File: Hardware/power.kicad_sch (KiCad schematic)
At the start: 17 parts, among them J1 I2C Debug, J2 I2C, J3 I2C, U3 LM285D-2.5, U7 AP7312-1833W6-7

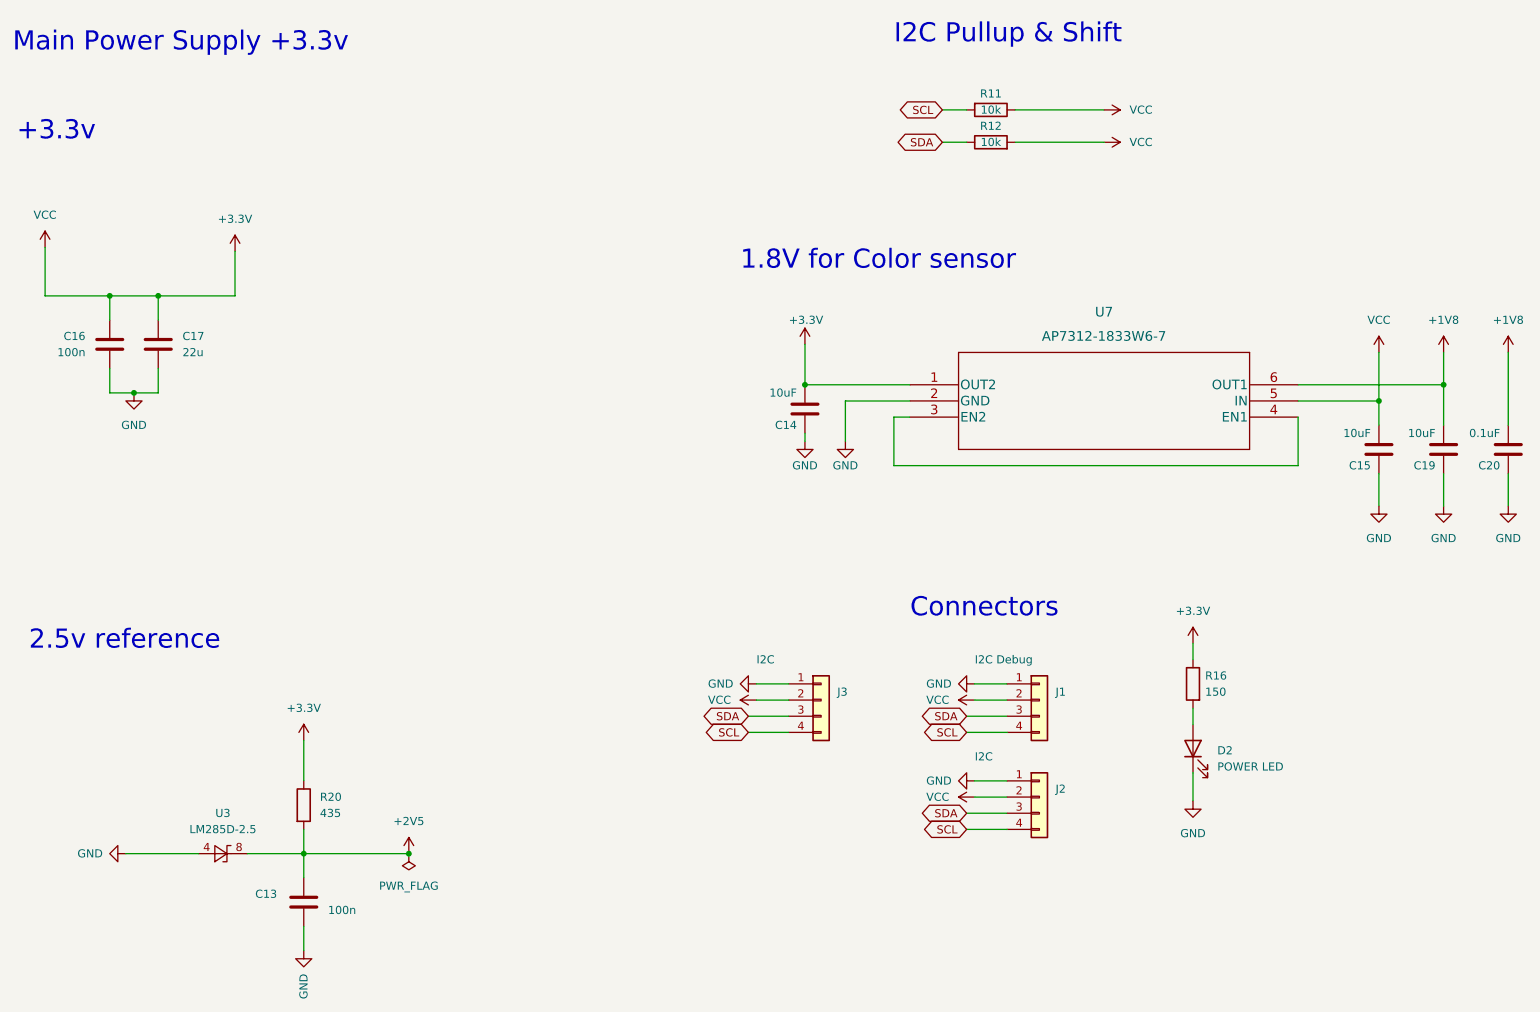
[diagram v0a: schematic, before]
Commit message: Version 0.6 - 4 layer version
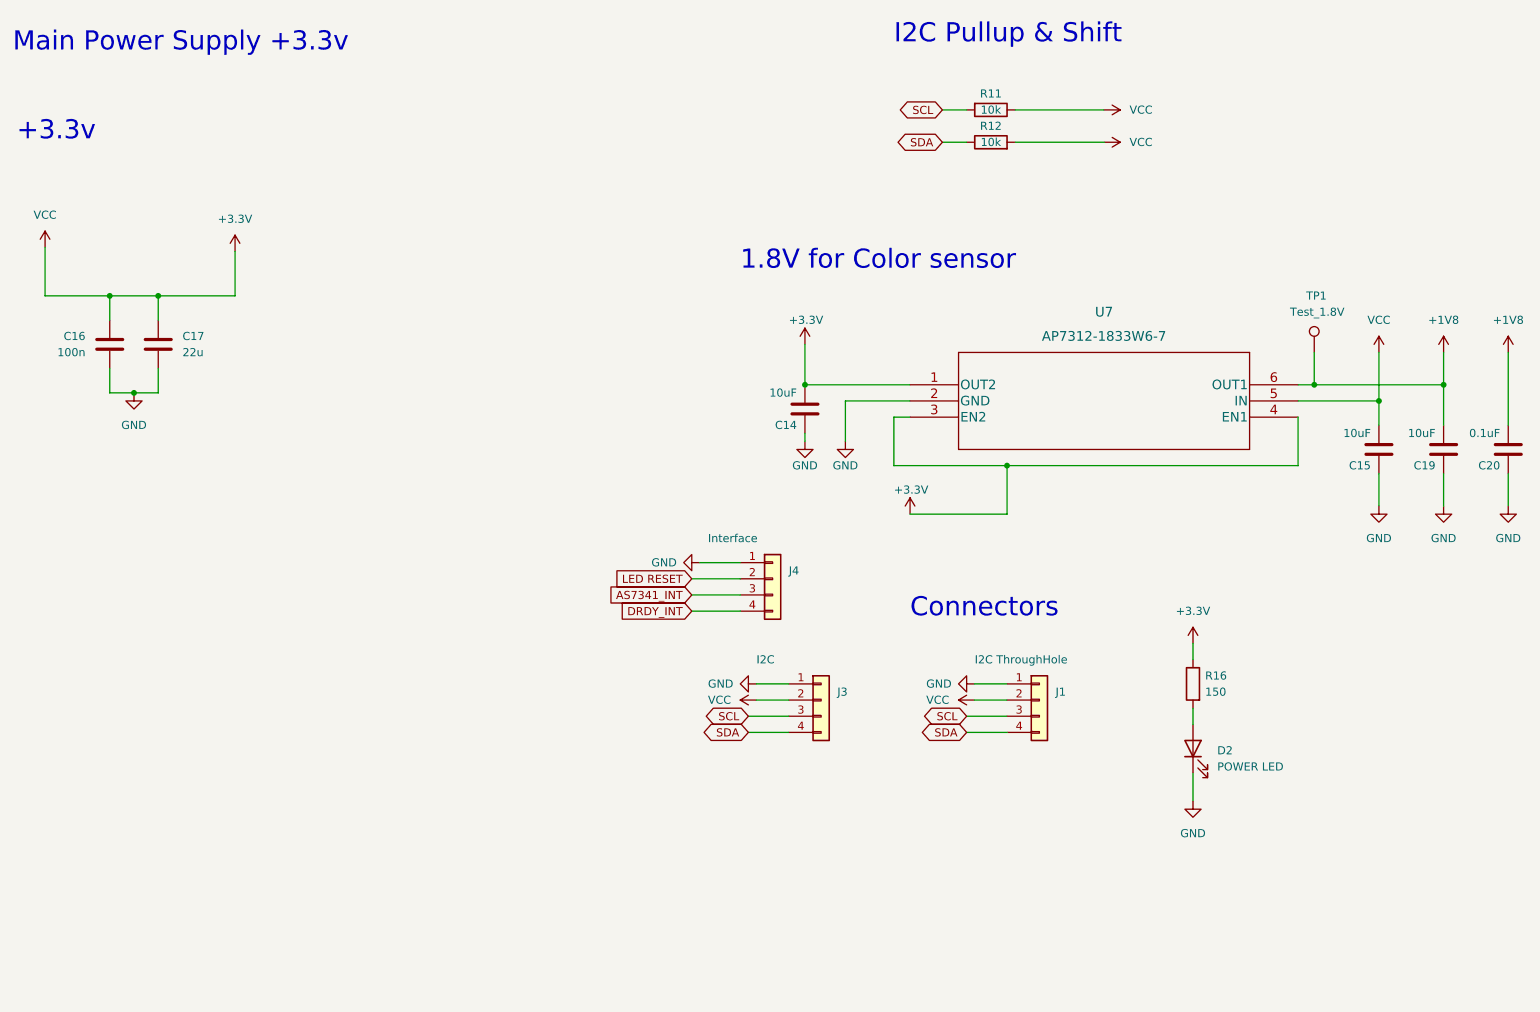
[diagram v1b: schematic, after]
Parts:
- removed C13: 100n, Capacitor_SMD:C_0603_1608Metric_Pad1.08x0.95mm_HandSolder, symbol Device:C
- removed J2: I2C, Connector_JST:JST_SH_SM04B-SRSS-TB_1x04-1MP_P1.00mm_Horizontal, symbol Connector_Generic:Conn_01x04
- removed R20: 435, Resistor_SMD:R_0603_1608Metric_Pad0.98x0.95mm_HandSolder, symbol Device:R
- removed U3: LM285D-2.5, Package_SO:SOIC-8_3.9x4.9mm_P1.27mm, symbol Reference_Voltage:LM285D-2.5
- added J4: Interface, Connector_PinSocket_2.54mm:PinSocket_1x04_P2.54mm_Vertical, symbol Connector_Generic:Conn_01x04
- added TP1: Test_1.8V, TestPoint:TestPoint_Pad_D1.5mm, symbol Connector:TestPoint
- J1: value I2C Debug -> I2C ThroughHole; footprint Connector_PinHeader_2.54mm:PinHeader_1x04_P2.54mm_Vertical -> Connector_PinSocket_2.54mm:PinSocket_1x04_P2.54mm_Vertical
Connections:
- net +1V8: now also TP1.1
- net +3V3: now also U7.3 (EN2), U7.4 (EN1)
- net GND: now also J4.1 (Pin_1)
- net SCL: now also J1.3 (Pin_3), J3.3 (Pin_3); no longer J1.4 (Pin_4), J3.4 (Pin_4)
- net SDA: now also J1.4 (Pin_4), J3.4 (Pin_4); no longer J1.3 (Pin_3), J3.3 (Pin_3)
- new net AS7341_INT: J4.3 (Pin_3)
- new net DRDY_INT: J4.4 (Pin_4)
- new net LED RESET: J4.2 (Pin_2)
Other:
- note removed: "2.5v reference"
